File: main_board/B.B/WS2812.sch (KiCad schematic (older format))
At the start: 120 parts, among them U1 WS2812, U10 WS2812, U11 WS2812, U12 WS2812, U13 WS2812, U14 WS2812, U15 WS2812, U16 WS2812, U17 WS2812, U18 WS2812, U19 WS2812, U2 WS2812, U20 WS2812, U21 WS2812, U22 WS2812, U23 WS2812, U24 WS2812, U25 WS2812, U26 WS2812, U27 WS2812, U28 WS2812, U29 WS2812, U3 WS2812, U30 WS2812, U31 WS2812, U32 WS2812, U33 WS2812, U34 WS2812, U35 WS2812, U36 WS2812, U37 WS2812, U38 WS2812, U39 WS2812, U4 WS2812, U40 WS2812, U41 WS2812, U42 WS2812, U43 WS2812, U44 WS2812, U45 WS2812, U46 WS2812, U47 WS2812, U48 WS2812, U49 WS2812, U5 WS2812, U50 WS2812, U51 WS2812, U52 WS2812, U53 WS2812, U54 WS2812, U55 WS2812, U56 WS2812, U57 WS2812, U58 WS2812, U59 WS2812, U6 WS2812, U60 WS2812, U7 WS2812, U8 WS2812, U9 WS2812

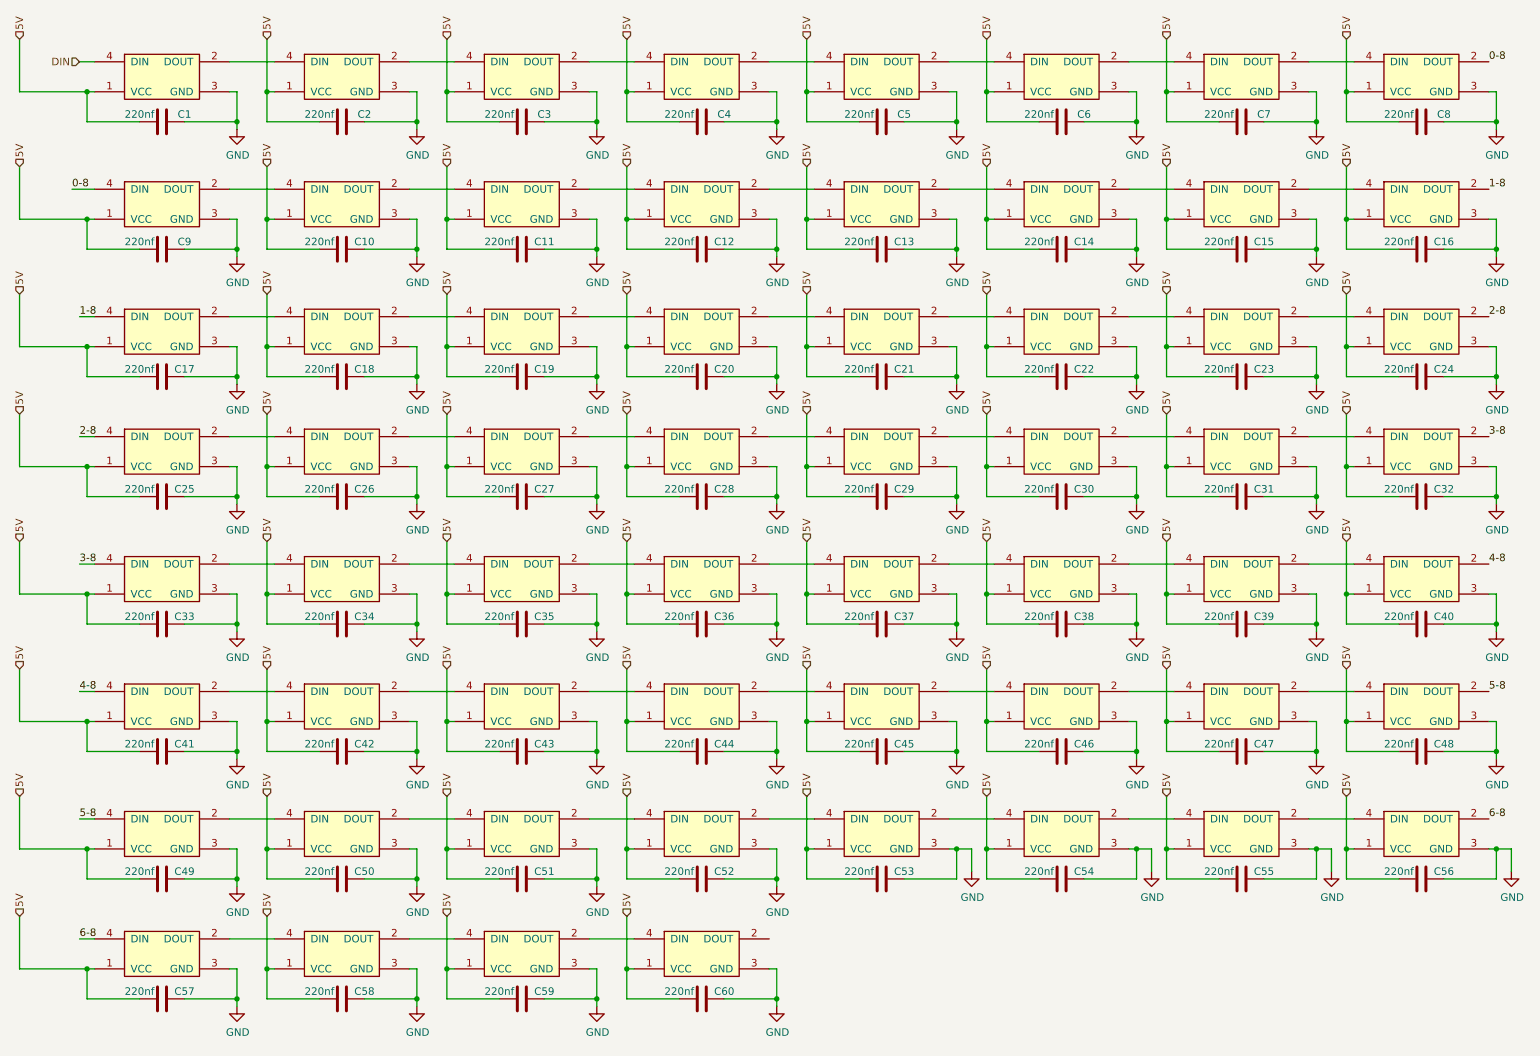
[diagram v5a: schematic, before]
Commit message: polifuse
-filtr k prijmaci IR
-merwni bterky -> za zapinani
-odstraneni odpojovani nabijecky + oprava napajeciho prouhu
-odstraneni prevodniku napeti k WS2812
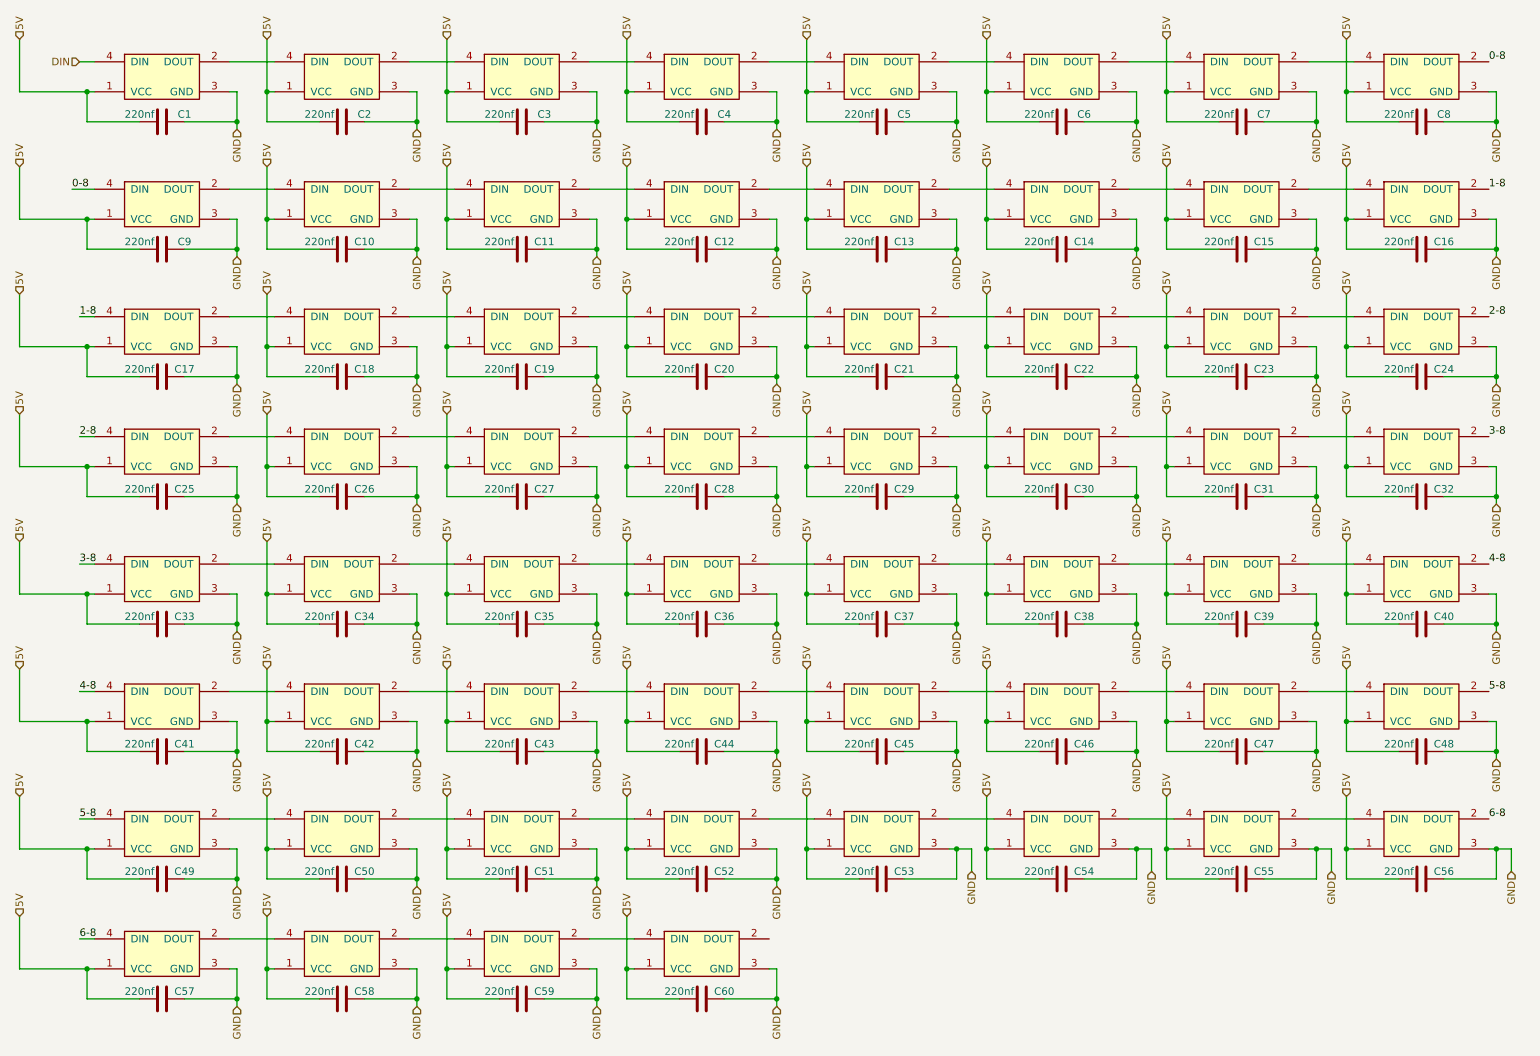
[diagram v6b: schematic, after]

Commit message: popisky
-popisky
-poladeni uddeleni enkoderu
-poladeni nayvu drah
-priopjeni gnd USB
-poligon V5 na led-desce do spodni vrstvu
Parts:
- C1, C10, C11, C12, C13, C14, C15, C16, C17, C18, C19, C2, C20, C21, C22, C23, C24, C25, C26, C27, C28, C29, C3, C30, C31, C32, C33, C34, C35, C36, C37, C38, C39, C4, C40, C41, C42, C43, C44, C45, C46, C47, C48, C49, C5, C50, C51, C52, C53, C54, C55, C56, C57, C58, C59, C6, C60, C7, C8, C9: symbol Device:C -> B.B-rescue:C-Device
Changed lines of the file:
@@
 EESchema Schematic File Version 4
-LIBS:B.B-cache
-EELAYER 29 0
+EELAYER 30 0
 EELAYER END
 $Descr A4 11693 8268
@@
 	900  1100 1350 1100
 $Comp
-L Device:C C1
+L B.B-rescue:C-Device C1
 U 1 1 5FAB9594
 P 1850 1300
@@
 5V
 $Comp
-L Device:C C2
+L B.B-rescue:C-Device C2
 U 1 1 5FAC4561
 P 3050 1300
@@
 $EndComp
 $Comp
-L Device:C C3
+L B.B-rescue:C-Device C3
 U 1 1 5FAC4874
 P 4250 1300
@@
 5V
 $Comp
-L Device:C C4
+L B.B-rescue:C-Device C4
 U 1 1 5FAC6087
 P 5450 1300
@@
 5V
 $Comp
-L Device:C C5
+L B.B-rescue:C-Device C5
 U 1 1 5FAC7F7D
 P 6650 1300
@@
 5V
 $Comp
-L Device:C C6
+L B.B-rescue:C-Device C6
 U 1 1 5FAC7F9C
 P 7850 1300
@@
 5V
 $Comp
-L Device:C C7
+L B.B-rescue:C-Device C7
 U 1 1 5FB2FBE5
 P 9050 1300
@@
 5V
 $Comp
-L Device:C C8
+L B.B-rescue:C-Device C8
 U 1 1 5FB2FC04
 P 10250 1300
@@
 $EndComp
 $Comp
-L Device:C C16
+L B.B-rescue:C-Device C16
 U 1 1 5FB47DD7
 P 10250 2150
@@
 	9750 1950 9750 2150
 $Comp
-L Device:C C15
+L B.B-rescue:C-Device C15
 U 1 1 5FB47DB8
 P 9050 2150
@@
 	8550 1950 8550 2150
 $Comp
-L Device:C C14
+L B.B-rescue:C-Device C14
 U 1 1 5FB47D99
 P 7850 2150
@@
 	7350 1950 7350 2150
 $Comp
-L Device:C C13
+L B.B-rescue:C-Device C13
 U 1 1 5FB47D7A
 P 6650 2150
@@
 	6150 1950 6150 2150
 $Comp
-L Device:C C12
+L B.B-rescue:C-Device C12
 U 1 1 5FB47D5B
 P 5450 2150
@@
 	4950 1950 4950 2150
 $Comp
-L Device:C C11
+L B.B-rescue:C-Device C11
 U 1 1 5FB47D3C
 P 4250 2150
@@
 $EndComp
 $Comp
-L Device:C C10
+L B.B-rescue:C-Device C10
 U 1 1 5FB47D35
 P 3050 2150
@@
 	1350 1950 1350 2150
 $Comp
-L Device:C C9
+L B.B-rescue:C-Device C9
 U 1 1 5FB47CEF
 P 1850 2150
@@
 	900  2800 1350 2800
 $Comp
-L Device:C C17
+L B.B-rescue:C-Device C17
 U 1 1 5FB8EEB1
 P 1850 3000
@@
 5V
 $Comp
-L Device:C C18
+L B.B-rescue:C-Device C18
 U 1 1 5FB8EEF7
 P 3050 3000
@@
 $EndComp
 $Comp
-L Device:C C19
+L B.B-rescue:C-Device C19
 U 1 1 5FB8EEFE
 P 4250 3000
@@
 5V
 $Comp
-L Device:C C20
+L B.B-rescue:C-Device C20
 U 1 1 5FB8EF1D
 P 5450 3000
@@
 5V
 $Comp
-L Device:C C21
+L B.B-rescue:C-Device C21
 U 1 1 5FB8EF3C
 P 6650 3000
@@
 5V
 $Comp
-L Device:C C22
+L B.B-rescue:C-Device C22
 U 1 1 5FB8EF5B
 P 7850 3000
@@
 5V
 $Comp
-L Device:C C23
+L B.B-rescue:C-Device C23
 U 1 1 5FB8EF7A
 P 9050 3000
@@
 5V
 $Comp
-L Device:C C24
+L B.B-rescue:C-Device C24
 U 1 1 5FB8EF99
 P 10250 3000
@@
 	900  3600 1350 3600
 $Comp
-L Device:C C25
+L B.B-rescue:C-Device C25
 U 1 1 5FB9FAD6
 P 1850 3800
@@
 	3500 3400 3800 3400
 $Comp
-L Device:C C26
+L B.B-rescue:C-Device C26
 U 1 1 5FB9FB1C
 P 3050 3800
@@
 $EndComp
 $Comp
-L Device:C C27
+L B.B-rescue:C-Device C27
 U 1 1 5FB9FB23
 P 4250 3800
@@
 	4700 3400 5000 3400
 $Comp
-L Device:C C28
+L B.B-rescue:C-Device C28
 U 1 1 5FB9FB42
 P 5450 3800
@@
 	5900 3400 6200 3400
 $Comp
-L Device:C C29
+L B.B-rescue:C-Device C29
 U 1 1 5FB9FB61
 P 6650 3800
@@
 	7100 3400 7400 3400
 $Comp
-L Device:C C30
+L B.B-rescue:C-Device C30
 U 1 1 5FB9FB80
 P 7850 3800
@@
 	8300 3400 8600 3400
 $Comp
-L Device:C C31
+L B.B-rescue:C-Device C31
 U 1 1 5FB9FB9F
 P 9050 3800
@@
 	9500 3400 9800 3400
 $Comp
-L Device:C C32
+L B.B-rescue:C-Device C32
 U 1 1 5FB9FBBE
 P 10250 3800
@@
 	900  4450 1350 4450
 $Comp
-L Device:C C33
+L B.B-rescue:C-Device C33
 U 1 1 5FC053DE
 P 1850 4650
@@
 5V
 $Comp
-L Device:C C34
+L B.B-rescue:C-Device C34
 U 1 1 5FC05424
 P 3050 4650
@@
 $EndComp
 $Comp
-L Device:C C35
+L B.B-rescue:C-Device C35
 U 1 1 5FC0542B
 P 4250 4650
@@
 5V
 $Comp
-L Device:C C36
+L B.B-rescue:C-Device C36
 U 1 1 5FC0544A
 P 5450 4650
@@
 5V
 $Comp
-L Device:C C37
+L B.B-rescue:C-Device C37
 U 1 1 5FC05469
 P 6650 4650
@@
 5V
 $Comp
-L Device:C C38
+L B.B-rescue:C-Device C38
 U 1 1 5FC05488
 P 7850 4650
@@
 5V
 $Comp
-L Device:C C39
+L B.B-rescue:C-Device C39
 U 1 1 5FC054A7
 P 9050 4650
@@
 5V
 $Comp
-L Device:C C40
+L B.B-rescue:C-Device C40
 U 1 1 5FC054C6
 P 10250 4650
@@
 $EndComp
 $Comp
-L Device:C C48
+L B.B-rescue:C-Device C48
 U 1 1 5FC054CD
 P 10250 5500
@@
 	9750 5300 9750 5500
 $Comp
-L Device:C C47
+L B.B-rescue:C-Device C47
 U 1 1 5FC054EC
 P 9050 5500
@@
 	8550 5300 8550 5500
 $Comp
-L Device:C C46
+L B.B-rescue:C-Device C46
 U 1 1 5FC0550B
 P 7850 5500
@@
 	7350 5300 7350 5500
 $Comp
-L Device:C C45
+L B.B-rescue:C-Device C45
 U 1 1 5FC0552A
 P 6650 5500
@@
 	6150 5300 6150 5500
 $Comp
-L Device:C C44
+L B.B-rescue:C-Device C44
 U 1 1 5FC05549
 P 5450 5500
@@
 	4950 5300 4950 5500
 $Comp
-L Device:C C43
+L B.B-rescue:C-Device C43
 U 1 1 5FC05568
 P 4250 5500
@@
 $EndComp
 $Comp
-L Device:C C42
+L B.B-rescue:C-Device C42
 U 1 1 5FC0556F
 P 3050 5500
@@
 	1350 5300 1350 5500
 $Comp
-L Device:C C41
+L B.B-rescue:C-Device C41
 U 1 1 5FC055B5
 P 1850 5500
@@
 	900  6150 1350 6150
 $Comp
-L Device:C C49
+L B.B-rescue:C-Device C49
 U 1 1 5FC055D2
 P 1850 6350
@@
 5V
 $Comp
-L Device:C C50
+L B.B-rescue:C-Device C50
 U 1 1 5FC05618
 P 3050 6350
@@
 $EndComp
 $Comp
-L Device:C C51
+L B.B-rescue:C-Device C51
 U 1 1 5FC0561F
 P 4250 6350
@@
 5V
 $Comp
-L Device:C C52
+L B.B-rescue:C-Device C52
 U 1 1 5FC0563E
 P 5450 6350
@@
 5V
 $Comp
-L Device:C C53
+L B.B-rescue:C-Device C53
 U 1 1 5FC0565D
 P 6650 6350
@@
 5V
 $Comp
-L Device:C C54
+L B.B-rescue:C-Device C54
 U 1 1 5FC0567C
 P 7850 6350
@@
 5V
 $Comp
-L Device:C C55
+L B.B-rescue:C-Device C55
 U 1 1 5FC0569B
 P 9050 6350
@@
 5V
 $Comp
-L Device:C C56
+L B.B-rescue:C-Device C56
 U 1 1 5FC056BA
 P 10250 6350
@@
 	900  6950 1350 6950
 $Comp
-L Device:C C57
+L B.B-rescue:C-Device C57
 U 1 1 5FC056CC
 P 1850 7150
@@
 	3500 6750 3800 6750
 $Comp
-L Device:C C58
+L B.B-rescue:C-Device C58
 U 1 1 5FC05712
 P 3050 7150
@@
 $EndComp
 $Comp
-L Device:C C59
+L B.B-rescue:C-Device C59
 U 1 1 5FC05719
 P 4250 7150
@@
 	4700 6750 5000 6750
 $Comp
-L Device:C C60
+L B.B-rescue:C-Device C60
 U 1 1 5FC05738
 P 5450 7150
